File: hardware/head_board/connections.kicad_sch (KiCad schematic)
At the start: 3 parts, among them J1 8P8C, J2 CAM, J6 CAMLED

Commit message: v1 revision to the schematic
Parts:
- added C?: 100n, Capacitor_SMD:C_0402_1005Metric_Pad0.74x0.62mm_HandSolder, symbol Device:C_Small
- added D? (x2): ESD, Capacitor_SMD:C_0603_1608Metric_Pad1.08x0.95mm_HandSolder, symbol Device:D_TVS_Filled
- added J?: Qwiic, Connector_JST:JST_PH_S4B-PH-SM4-TB_1x04-1MP_P2.00mm_Horizontal, symbol Connector_Generic:Conn_01x04
- added J?: AUX, Connector_JST:JST_XH_B3B-XH-AM_1x03_P2.50mm_Vertical, symbol Connector_Generic:Conn_01x03
- added R? (x2): 10K, Resistor_SMD:R_0402_1005Metric_Pad0.72x0.64mm_HandSolder, symbol Device:R_US
- added R? (x2): 2.2k, Resistor_SMD:R_0402_1005Metric_Pad0.72x0.64mm_HandSolder, symbol Device:R_US
- added U? (x2): TVS, Package_TO_SOT_SMD:SOT-23-6, symbol winterbloom:USBLC6-2SC6
- added U?: 74HC2G34, Package_TO_SOT_SMD:SOT-363_SC-70-6, symbol winterbloom:74HC2G34
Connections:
- net +5V: now also C?.1, J?.2 (Pin_2), U?.5 (VBUS), U?.5 (VBUS), U?.5 (VCC)
- net CAM_D+: now also U?.3 (D+), U?.4 (D+)
- net CAM_D-: now also U?.1 (D-), U?.6 (D-)
- net CAM_LED: now also R?.2, U?.1 (1A); no longer J6.1 (Pin_1)
- net GND: now also C?.2, D?.1 (A1), D?.1 (A1), J?.3 (Pin_3), R?.1, R?.1, U?.2 (GND), U?.2 (GND), U?.2 (GND)
- net MCU_D+: now also U?.3 (D+), U?.4 (D+)
- net MCU_D-: now also U?.1 (D-), U?.6 (D-)
- net +24V renamed VDC
- new net: J6.1 (Pin_1), U?.6 (1Y)
- new net: J?.1 (Pin_1), U?.4 (2Y)
- new net +3V3: J?.2 (Pin_2), R?.2, R?.2
- new net AUX_OUT: R?.2, U?.3 (2A)
- new net QWIIC_SCL: D?.2 (A2), J?.4 (Pin_4), R?.1
- new net QWIIC_SDA: D?.2 (A2), J?.3 (Pin_3), R?.1
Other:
- note added: "* 74HC2G34 has built-in ESD protection"
- note added: "* Make sure TVS diodes are close to J1 * Route camera USB pair over uninterrupted ground plane"
- note added: "5V outputs"
- note added: "CAT6, USB TVS, and camera header"
- note added: "Qwiic"
- company: (none) -> Winterbloom
- title: (none) -> Candela Head
- moved on the sheet: J1, J2, J6

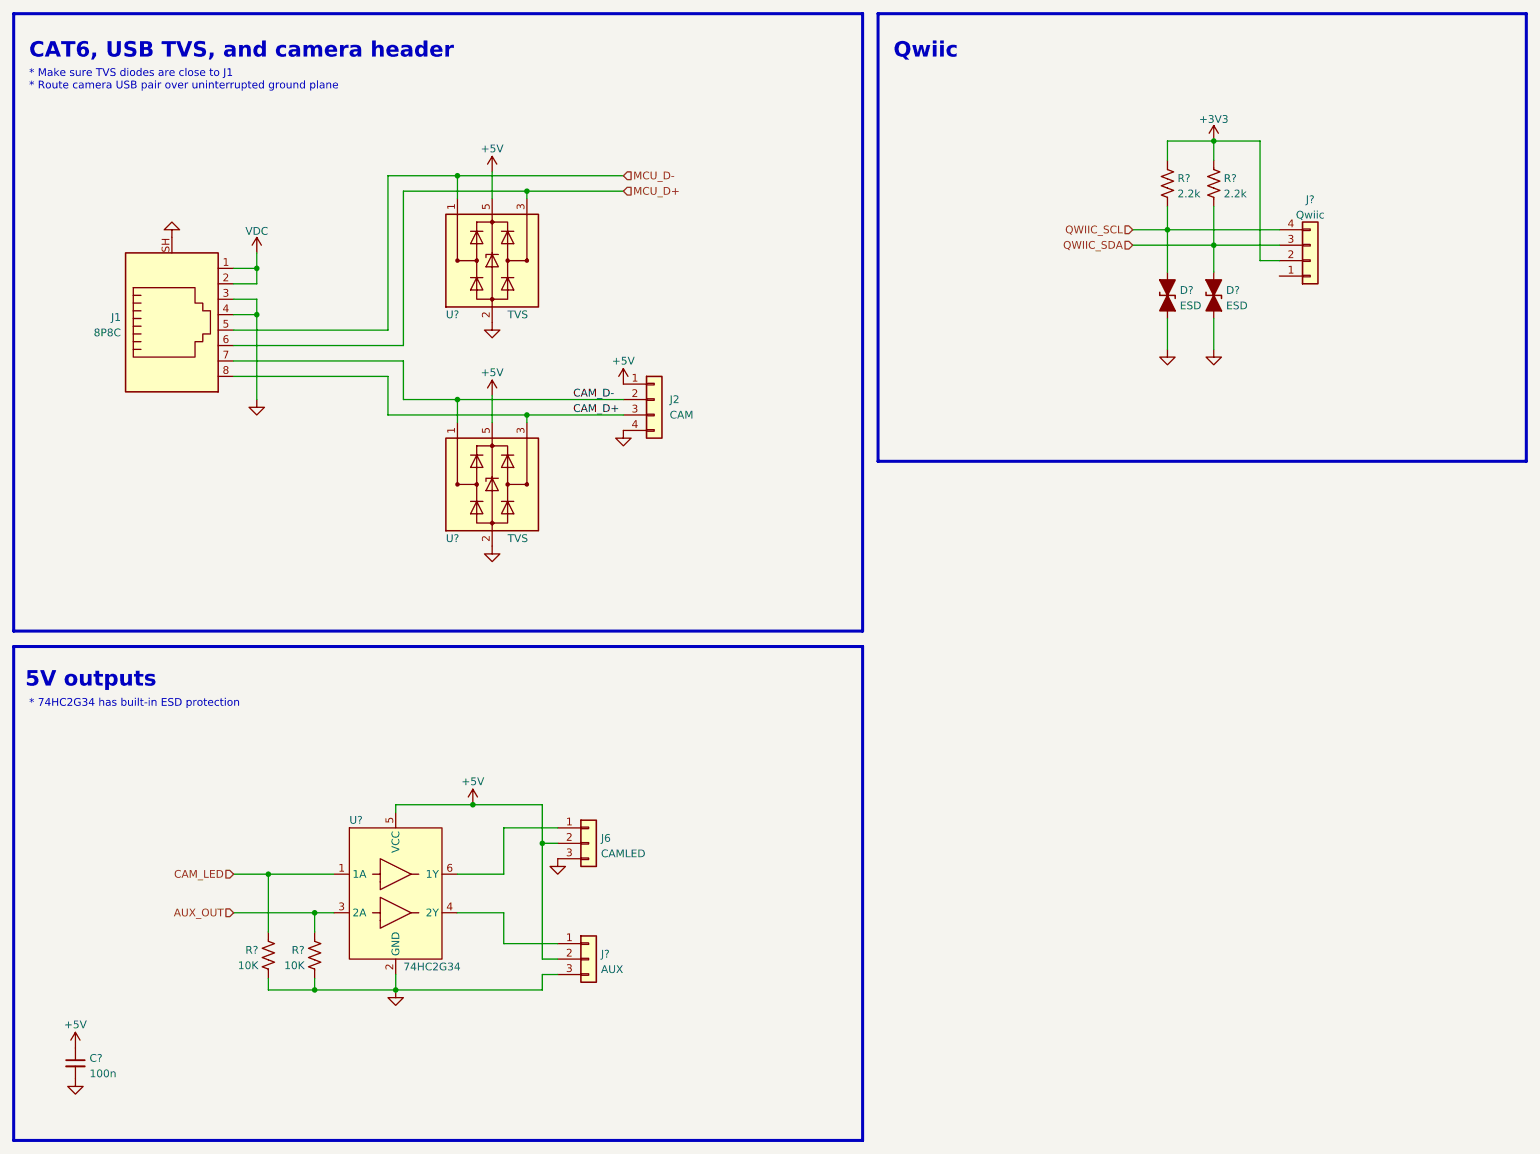
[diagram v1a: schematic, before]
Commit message: Footprints assigned
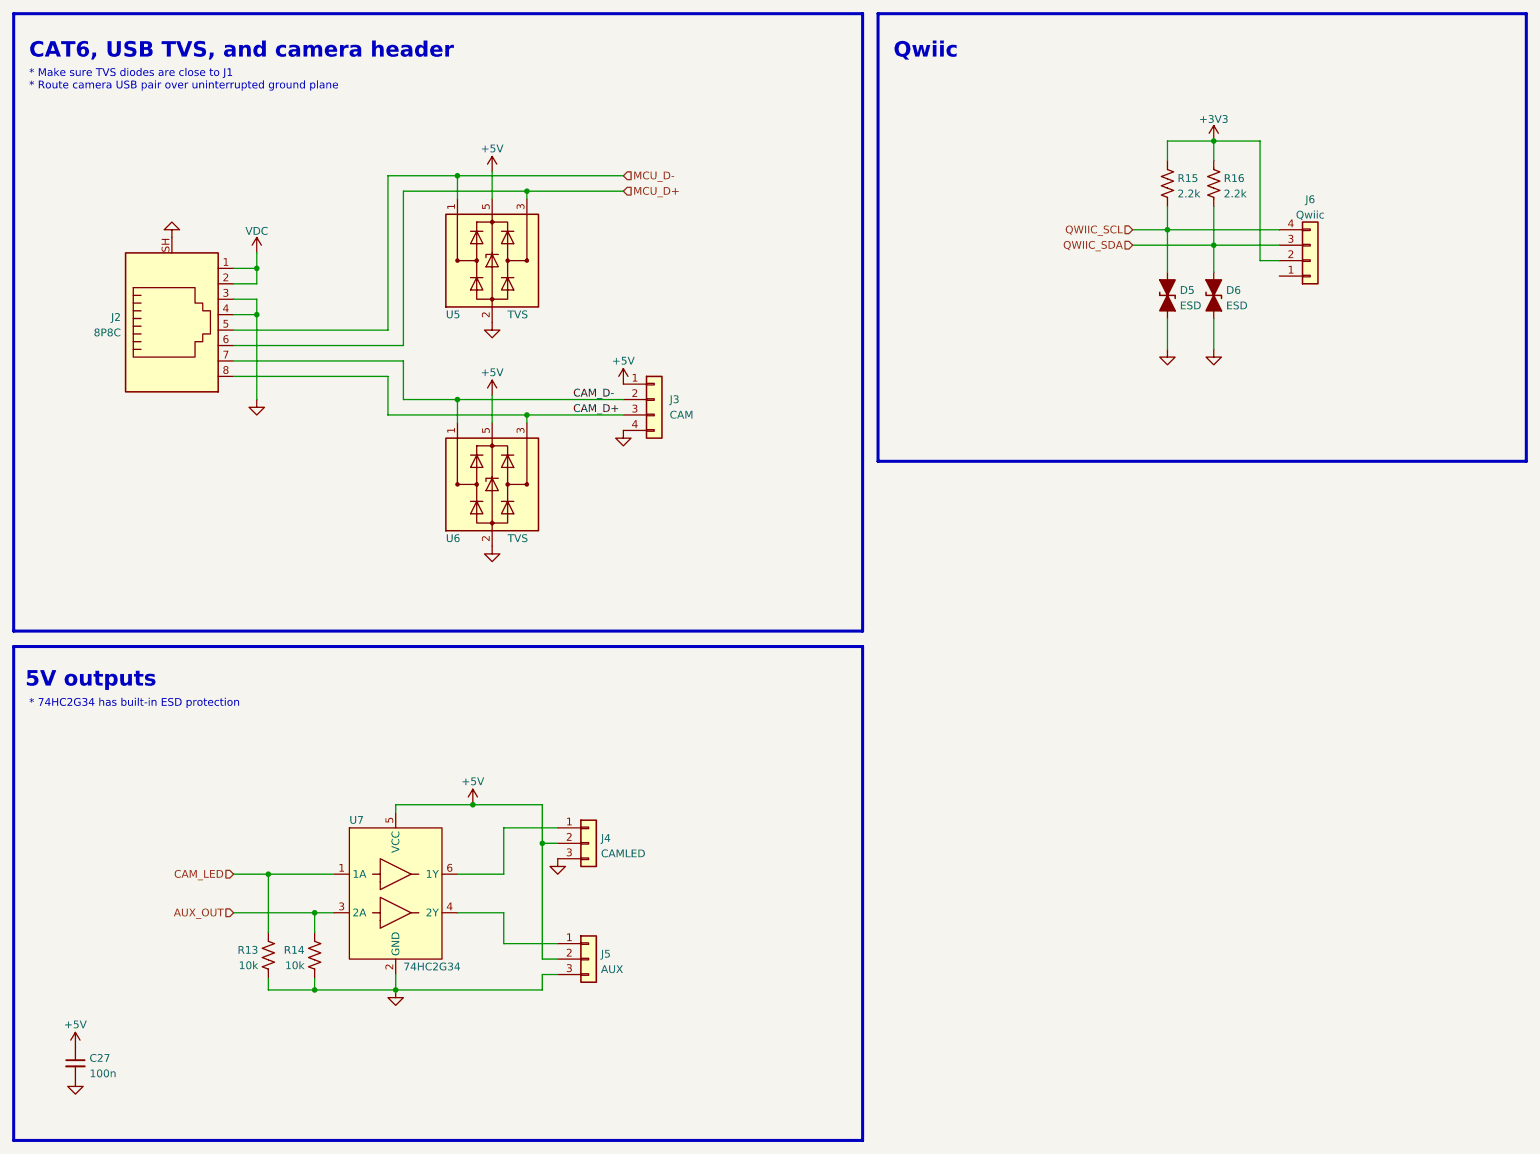
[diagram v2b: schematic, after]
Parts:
- C27: renamed from C?; Rating 16V -> 10V
- R13, R14: renamed from R?; value 10K -> 10k; Rating (none) -> 63mW
- R15, R16: renamed from R?; Rating (none) -> 63mW
- gave numbers to parts that had none: 7
- renumbered J1 to J2, J2 to J3, J6 to J4

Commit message: Finish up layout for v1, ended up removing some stuff
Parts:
- removed D5, D6: ESD, Capacitor_SMD:C_0603_1608Metric_Pad1.08x0.95mm_HandSolder, symbol Device:D_TVS_Filled
- removed J6: Qwiic, Connector_JST:JST_PH_S4B-PH-SM4-TB_1x04-1MP_P2.00mm_Horizontal, symbol Connector_Generic:Conn_01x04
- removed R15, R16: 2.2k, Resistor_SMD:R_0402_1005Metric_Pad0.72x0.64mm_HandSolder, symbol Device:R_US
- J2: footprint winterbloom:Connector_RJ45_SS-7188S-A-PG4-BA-50 -> winterbloom:Connector_RJ45_ASSMANN_A-2014-2S-4-N-R; mpn SS-7188S-A-PG4-BA-50 -> A-2014-2S-4-N-R
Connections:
- net CAM_D+: now also J2.6, U5.3 (D+), U5.4 (D+); no longer J2.8, U6.3 (D+), U6.4 (D+)
- net CAM_D-: now also J2.5, U5.1 (D-), U5.6 (D-); no longer J2.7, U6.1 (D-), U6.6 (D-)
- net MCU_D+: now also J2.8, U6.3 (D+), U6.4 (D+); no longer J2.6, U5.3 (D+), U5.4 (D+)
- net MCU_D-: now also J2.7, U6.1 (D-), U6.6 (D-); no longer J2.5, U5.1 (D-), U5.6 (D-)
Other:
- note removed: "Qwiic"
- moved on the sheet: J3

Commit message: V2 of the head board (Jellyfish)
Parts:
- removed J2: 8P8C, winterbloom:Connector_RJ45_ASSMANN_A-2014-2S-4-N-R, symbol Connector:8P8C_Shielded
- removed J3: CAM, Connector_JST:JST_XH_B4B-XH-AM_1x04_P2.50mm_Vertical, symbol Connector_Generic:Conn_01x04
- removed J4: CAMLED, Connector_JST:JST_XH_B3B-XH-AM_1x03_P2.50mm_Vertical, symbol Connector_Generic:Conn_01x03
- removed J5: AUX, Connector_JST:JST_XH_B3B-XH-AM_1x03_P2.50mm_Vertical, symbol Connector_Generic:Conn_01x03
- removed U5: TVS, Package_TO_SOT_SMD:SOT-23-6, symbol winterbloom:USBLC6-2SC6
- added C1: 100n, Capacitor_SMD:C_0402_1005Metric_Pad0.74x0.62mm_HandSolder, symbol Device:C_Small
- added J1: INS, Connector_JST:JST_SH_BM04B-SRSS-TB_1x04-1MP_P1.00mm_Vertical, symbol Connector_Generic_MountingPin:Conn_01x04_MountingPin
- added J10: Stemma QT, Connector_JST:JST_SH_BM04B-SRSS-TB_1x04-1MP_P1.00mm_Vertical, symbol Connector_Generic_MountingPin:Conn_01x04_MountingPin
- added J2: 8P8C_LED_Shielded, winterbloom:RJ45_Amphenol_RJE45-188-1411_Vertical, symbol Connector:8P8C_LED_Shielded
- added J3: CAM, Connector_JST:JST_SH_BM04B-SRSS-TB_1x04-1MP_P1.00mm_Vertical, symbol Connector_Generic_MountingPin:Conn_01x04_MountingPin
- added J4: CAMLED, Connector_JST:JST_SH_BM03B-SRSS-TB_1x03-1MP_P1.00mm_Vertical, symbol Connector_Generic_MountingPin:Conn_01x03_MountingPin
- added J5: OUT1, Connector_JST:JST_SH_BM03B-SRSS-TB_1x03-1MP_P1.00mm_Vertical, symbol Connector_Generic_MountingPin:Conn_01x03_MountingPin
- added J6: BLTOUCH, Connector_JST:JST_SH_BM05B-SRSS-TB_1x05-1MP_P1.00mm_Vertical, symbol Connector_Generic_MountingPin:Conn_01x05_MountingPin
- added R1, R15, R2, R26, R27: 5.1k, Resistor_SMD:R_0402_1005Metric_Pad0.72x0.64mm_HandSolder, symbol Device:R_US
- added R16, R3: 100, Resistor_SMD:R_0402_1005Metric_Pad0.72x0.64mm_HandSolder, symbol Device:R_US
- added U5: 74HC2G34, Package_TO_SOT_SMD:SOT-363_SC-70-6, symbol winterbloom:74HC2G34
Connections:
- net +5V: now also J1.1 (Pin_1), J3.1 (Pin_1), J4.2 (Pin_2), J5.2 (Pin_2), J6.4 (Pin_4), R1.2
- net CAM_D+: now also J2.1, J3.3 (Pin_3)
- net CAM_D-: now also J2.2, J3.2 (Pin_2)
- net GND: now also C1.2, J1.4 (Pin_4), J1.MP (MountPin), J10.1 (Pin_1), J10.MP (MountPin), J2.11, J2.3, J2.7, J2.9, J2.SH, J3.4 (Pin_4), J3.MP (MountPin), J4.3 (Pin_3), J4.MP (MountPin), J5.3 (Pin_3), J5.MP (MountPin), J6.2 (Pin_2), J6.5 (Pin_5), J6.MP (MountPin), U5.2 (GND)
- net MCU_D+: now also J2.4
- net MCU_D-: now also J2.5
- net VDC: now also J2.6, J2.8, R2.2
- net at U7.6 (1Y): now also J4.1 (Pin_1)
- net at U7.4 (2Y): now also J5.1 (Pin_1)
- new net: R16.1, U5.3 (2A)
- new net: J1.3 (Pin_3), R16.2
- new net: J1.2 (Pin_2), R3.2
- new net: J2.10, R1.1
- new net: J2.12, R2.1
- new net: R3.1, U5.1 (1A)
- new net +3V3: C1.1, J10.2 (Pin_2), R15.2, R26.2, R27.2, U5.5 (VCC)
- new net BLTOUCH_CONTROL: J6.3 (Pin_3)
- new net BLTOUCH_OUT: J6.1 (Pin_1), R15.1
- new net IN_1: U5.6 (1Y)
- new net IN_2: U5.4 (2Y)
- new net QWIIC_SCL: J10.4 (Pin_4), R27.1
- new net QWIIC_SDA: J10.3 (Pin_3), R26.1
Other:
- note added: "* Make sure TVS diodes are close to J1 * Route camera USB pair over uninterrupted ground plane * Note twisted pair wiring on Cat6 cable: 1. White/Green 2. Green 3. White/Orange 4. Blue 5. White/Blue 6. Orange 7. White/Brown 8. Brown"
- note added: "Black"
- note added: "Brown"
- note added: "Red"
- note added: "TODO: double check pinout"
- note added: "White"
- note added: "Yellow"
- note removed: "* Make sure TVS diodes are close to J1 * Route camera USB pair over uninterrupted ground plane"
- title: Candela Head -> Jellyfish
- moved on the sheet: U6

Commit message: Replace veritcal connectors with horizontal ones
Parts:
- J1, J10, J3: footprint Connector_JST:JST_SH_BM04B-SRSS-TB_1x04-1MP_P1.00mm_Vertical -> Connector_JST:JST_SH_SM04B-SRSS-TB_1x04-1MP_P1.00mm_Horizontal
- J4, J5: footprint Connector_JST:JST_SH_BM03B-SRSS-TB_1x03-1MP_P1.00mm_Vertical -> Connector_JST:JST_SH_SM03B-SRSS-TB_1x03-1MP_P1.00mm_Horizontal
- J6: footprint Connector_JST:JST_SH_BM05B-SRSS-TB_1x05-1MP_P1.00mm_Vertical -> Connector_JST:JST_SH_SM05B-SRSS-TB_1x05-1MP_P1.00mm_Horizontal
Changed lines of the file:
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@@
       (effects (font (size 1.27 1.27)) (justify left))
     )
-    (property "Footprint" "Connector_JST:JST_SH_BM04B-SRSS-TB_1x04-1MP_P1.00mm_Vertical" (id 2) (at 117.475 57.785 0)
+    (property "Footprint" "Connector_JST:JST_SH_SM04B-SRSS-TB_1x04-1MP_P1.00mm_Horizontal" (id 2) (at 117.475 57.785 0)
       (effects (font (size 1.27 1.27)) hide)
     )
@@
       (effects (font (size 1.27 1.27)) (justify left))
     )
-    (property "Footprint" "Connector_JST:JST_SH_BM04B-SRSS-TB_1x04-1MP_P1.00mm_Vertical" (id 2) (at 233.045 90.17 0)
+    (property "Footprint" "Connector_JST:JST_SH_SM04B-SRSS-TB_1x04-1MP_P1.00mm_Horizontal" (id 2) (at 233.045 90.17 0)
       (effects (font (size 1.27 1.27)) hide)
     )
@@
       (effects (font (size 1.27 1.27)) (justify left))
     )
-    (property "Footprint" "Connector_JST:JST_SH_BM03B-SRSS-TB_1x03-1MP_P1.00mm_Vertical" (id 2) (at 109.855 173.355 0)
+    (property "Footprint" "Connector_JST:JST_SH_SM03B-SRSS-TB_1x03-1MP_P1.00mm_Horizontal" (id 2) (at 109.855 173.355 0)
       (effects (font (size 1.27 1.27)) hide)
     )
@@
     (property "Reference" "J6" (id 0) (at 222.25 44.45 0))
     (property "Value" "BLTOUCH" (id 1) (at 222.25 46.99 0))
-    (property "Footprint" "Connector_JST:JST_SH_BM05B-SRSS-TB_1x05-1MP_P1.00mm_Vertical" (id 2) (at 222.25 55.88 0)
+    (property "Footprint" "Connector_JST:JST_SH_SM05B-SRSS-TB_1x05-1MP_P1.00mm_Horizontal" (id 2) (at 222.25 55.88 0)
       (effects (font (size 1.27 1.27)) hide)
     )
@@
     (property "Reference" "J1" (id 0) (at 189.23 127 0))
     (property "Value" "INS" (id 1) (at 189.23 129.54 0))
-    (property "Footprint" "Connector_JST:JST_SH_BM04B-SRSS-TB_1x04-1MP_P1.00mm_Vertical" (id 2) (at 189.23 136.525 0)
+    (property "Footprint" "Connector_JST:JST_SH_SM04B-SRSS-TB_1x04-1MP_P1.00mm_Horizontal" (id 2) (at 189.23 136.525 0)
       (effects (font (size 1.27 1.27)) hide)
     )
@@
       (effects (font (size 1.27 1.27)) (justify left))
     )
-    (property "Footprint" "Connector_JST:JST_SH_BM03B-SRSS-TB_1x03-1MP_P1.00mm_Vertical" (id 2) (at 109.855 151.765 0)
-      (effects (font (size 1.27 1.27)) hide)
-    )
+    (property "Footprint" "Connector_JST:JST_SH_SM03B-SRSS-TB_1x03-1MP_P1.00mm_Horizontal" (id 2) (at 109.855 151.765 0)
+      (effects (font (size 1.27 1.27)) hide)
+    )
